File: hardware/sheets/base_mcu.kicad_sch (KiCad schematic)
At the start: 23 parts, among them J1 DevKit J1 (left row), J2 DevKit J3 (right row), J3 Qwiic, J4 Qwiic, J5 Expansion 2x10

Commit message: hardware: chip resistors and ceramic capacitors on KiCad standard footprints (Decision #47); schematic, library and gapped copies regenerated, ERC 0 errors
Co-Authored-By: Claude Fable 5.1 <noreply@anthropic.com>
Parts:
- R1, R2, R3, R4: footprint class_board:R0603 -> Resistor_SMD:R_0603_1608Metric
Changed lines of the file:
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@@
     (property "Reference" "R1" (at 55.88 171.958 0) (show_name no) (effects (font (size 1.27 1.27)) (justify left bottom)))
     (property "Value" "33" (at 55.88 178.562 0) (show_name no) (effects (font (size 1.27 1.27)) (justify left top)))
-    (property "Footprint" "class_board:R0603" (at 59.69 175.26 0) (show_name no) (effects (font (size 1.27 1.27)) (hide yes)))
+    (property "Footprint" "Resistor_SMD:R_0603_1608Metric" (at 59.69 175.26 0) (show_name no) (effects (font (size 1.27 1.27)) (hide yes)))
     (property "Datasheet" "https://www.lcsc.com/product-detail/C23140.html" (at 59.69 175.26 0) (show_name no) (effects (font (size 1.27 1.27)) (hide yes)))
     (property "Description" "Resistor 33 1% 0603 100 mW (Uniroyal 0603WAF330JT5E)" (at 59.69 175.26 0) (show_name no) (effects (font (size 1.27 1.27)) (hide yes)))
@@
     (property "Reference" "R2" (at 55.88 182.118 0) (show_name no) (effects (font (size 1.27 1.27)) (justify left bottom)))
     (property "Value" "33" (at 55.88 188.722 0) (show_name no) (effects (font (size 1.27 1.27)) (justify left top)))
-    (property "Footprint" "class_board:R0603" (at 59.69 185.42 0) (show_name no) (effects (font (size 1.27 1.27)) (hide yes)))
+    (property "Footprint" "Resistor_SMD:R_0603_1608Metric" (at 59.69 185.42 0) (show_name no) (effects (font (size 1.27 1.27)) (hide yes)))
     (property "Datasheet" "https://www.lcsc.com/product-detail/C23140.html" (at 59.69 185.42 0) (show_name no) (effects (font (size 1.27 1.27)) (hide yes)))
     (property "Description" "Resistor 33 1% 0603 100 mW (Uniroyal 0603WAF330JT5E)" (at 59.69 185.42 0) (show_name no) (effects (font (size 1.27 1.27)) (hide yes)))
@@
     (property "Reference" "R3" (at 247.65 55.118 0) (show_name no) (effects (font (size 1.27 1.27)) (justify left bottom)))
     (property "Value" "4.7k" (at 247.65 64.262 0) (show_name no) (effects (font (size 1.27 1.27)) (justify left top)))
-    (property "Footprint" "class_board:R0603" (at 250.19 59.69 0) (show_name no) (effects (font (size 1.27 1.27)) (hide yes)))
+    (property "Footprint" "Resistor_SMD:R_0603_1608Metric" (at 250.19 59.69 0) (show_name no) (effects (font (size 1.27 1.27)) (hide yes)))
     (property "Datasheet" "https://www.lcsc.com/product-detail/C23162.html" (at 250.19 59.69 0) (show_name no) (effects (font (size 1.27 1.27)) (hide yes)))
     (property "Description" "Resistor 4.7k 1% 0603 100 mW (Uniroyal 0603WAF4701T5E)" (at 250.19 59.69 0) (show_name no) (effects (font (size 1.27 1.27)) (hide yes)))
@@
     (property "Reference" "R4" (at 260.35 55.118 0) (show_name no) (effects (font (size 1.27 1.27)) (justify left bottom)))
     (property "Value" "4.7k" (at 260.35 64.262 0) (show_name no) (effects (font (size 1.27 1.27)) (justify left top)))
-    (property "Footprint" "class_board:R0603" (at 262.89 59.69 0) (show_name no) (effects (font (size 1.27 1.27)) (hide yes)))
+    (property "Footprint" "Resistor_SMD:R_0603_1608Metric" (at 262.89 59.69 0) (show_name no) (effects (font (size 1.27 1.27)) (hide yes)))
     (property "Datasheet" "https://www.lcsc.com/product-detail/C23162.html" (at 262.89 59.69 0) (show_name no) (effects (font (size 1.27 1.27)) (hide yes)))
     (property "Description" "Resistor 4.7k 1% 0603 100 mW (Uniroyal 0603WAF4701T5E)" (at 262.89 59.69 0) (show_name no) (effects (font (size 1.27 1.27)) (hide yes)))

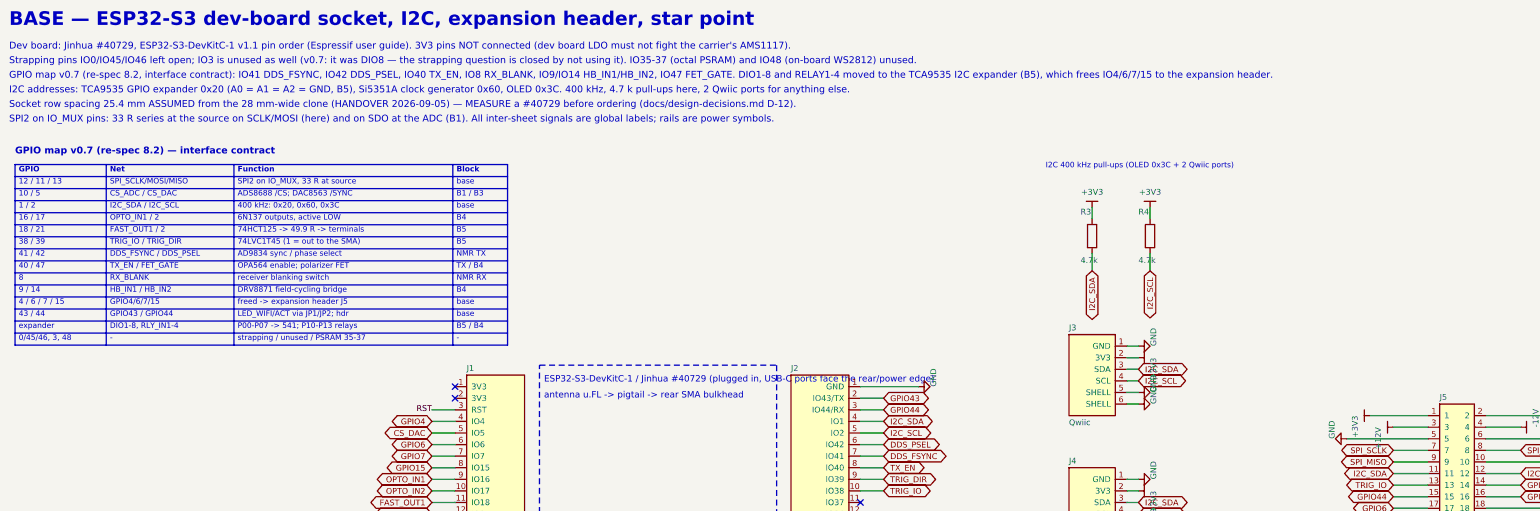
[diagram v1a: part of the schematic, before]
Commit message: hardware: panel stacked on the back (180 x 100, three 2x20 headers, 17 SMA, TTL strip, TX terminal, Qwiic); TTL/fast/TX-coil/Qwiic connectors leave the main board; mains-safe relay channels (JQC-3FF 10 A, MAINS net class + DRC rules); library, sheets, gapped copies, docs regenerated; ERC 0 errors
Decisions #45-#50 in the course repo. The main-board PCB is unchanged: Update PCB from Schematic, header placement, relay re-spacing and connector rotation are the instructor's GUI steps on the master.

Co-Authored-By: Claude Fable 5.1 <noreply@anthropic.com>
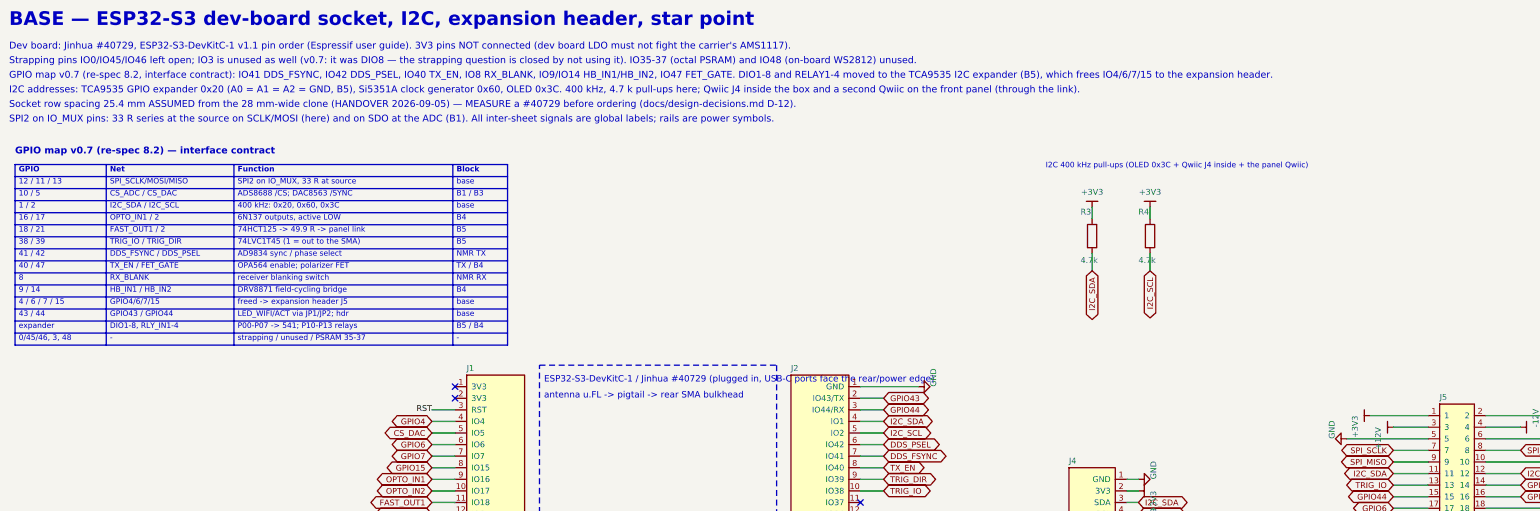
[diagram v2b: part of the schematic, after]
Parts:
- removed J3: Qwiic, class_board:CONN-SMD_4P-P1.00_XY-SM04B-SRSS-TB, symbol class_board:QWIIC_SM04B-SRSS
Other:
- note added: "74HCT125 -> 49.9 R -> panel link"
- note added: "I2C 400 kHz pull-ups (OLED 0x3C + Qwiic J4 inside + the panel Qwiic)"
- note added: "I2C addresses: TCA9535 GPIO expander 0x20 (A0 = A1 = A2 = GND, B5), Si5351A clock generator 0x60, OLED 0x3C. 400 kHz, 4.7 k pull-ups here; Qwiic J4 inside the box and a second Qwiic on the front panel (through the link)."
- note removed: "74HCT125 -> 49.9 R -> terminals"
- note removed: "I2C 400 kHz pull-ups (OLED 0x3C + 2 Qwiic ports)"
- note removed: "I2C addresses: TCA9535 GPIO expander 0x20 (A0 = A1 = A2 = GND, B5), Si5351A clock generator 0x60, OLED 0x3C. 400 kHz, 4.7 k pull-ups here, 2 Qwiic ports for anything else."

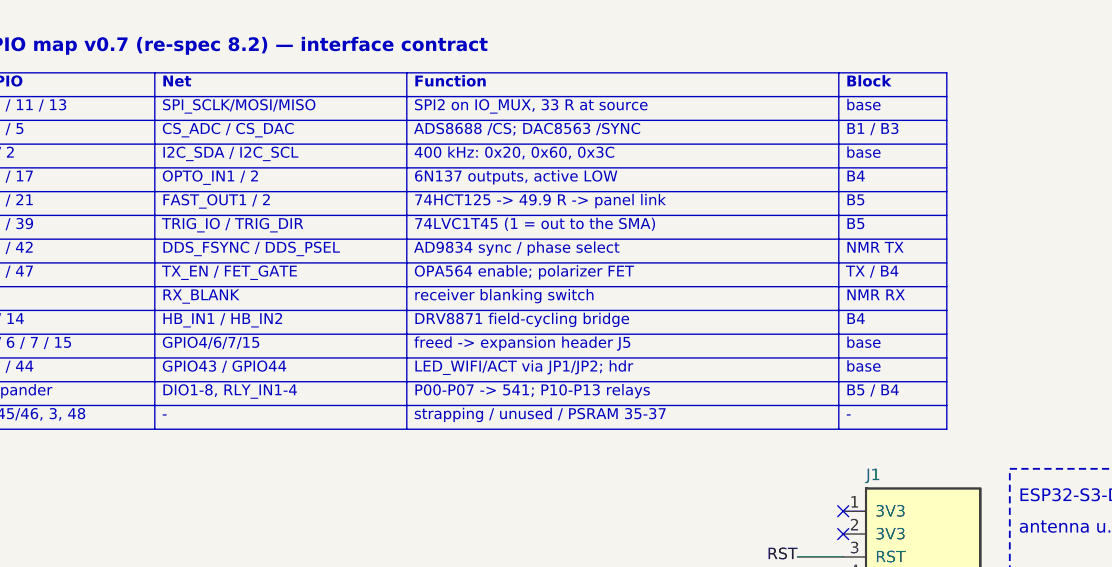
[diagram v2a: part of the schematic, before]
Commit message: v0.7d: relays and mains removed, MODULE OUT 1-7 (5 V TTL) on a shrouded 2x6 header on the front panel, isolated inputs moved to the panel, section C = the front-panel board (4-layer, 18 mm SMA grid, OLED clear of headers, unrouted student copy), main board re-placed; workbook, tutor guide, firmware docs, hardware docs updated (Decision #58)
Co-Authored-By: Claude Fable 5.1 <noreply@anthropic.com>
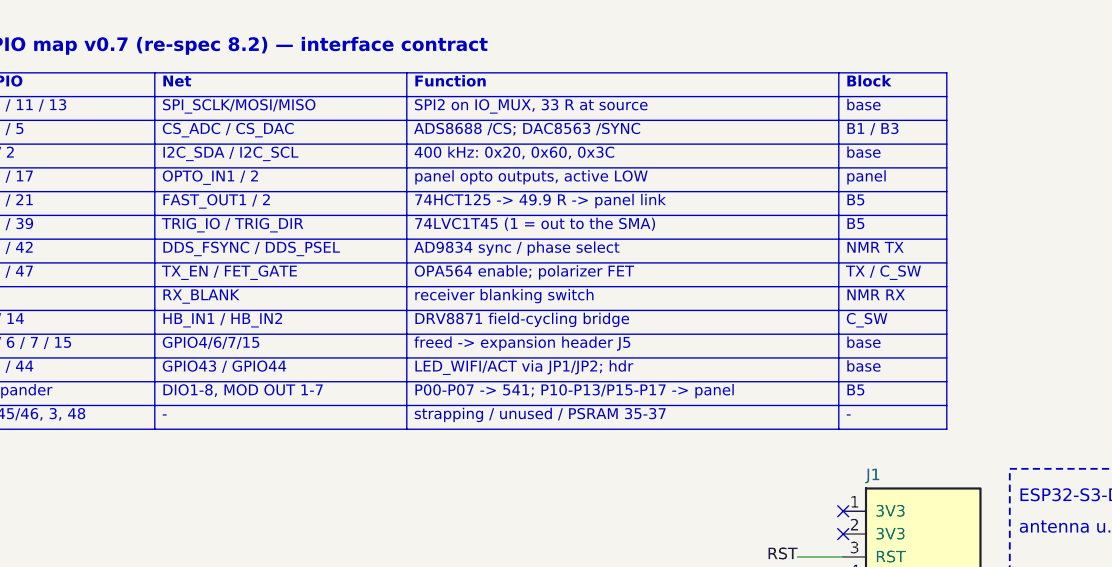
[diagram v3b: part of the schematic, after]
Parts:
- J5: footprint class_board:HDR-TH_20P-P2.54-V-M-R2-C10-S2.54 -> Connector_PinHeader_2.54mm:PinHeader_2x10_P2.54mm_Vertical
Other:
- note added: "C_SW"
- note added: "DIO1-8, MOD OUT 1-7"
- note added: "P00-P07 -> 541; P10-P13/P15-P17 -> panel"
- note added: "TX / C_SW"
- note added: "panel"
- note added: "panel opto outputs, active LOW"
- note removed: "6N137 outputs, active LOW"
- note removed: "B4"
- note removed: "B5 / B4"
- note removed: "DIO1-8, RLY_IN1-4"
- note removed: "P00-P07 -> 541; P10-P13 relays"
- note removed: "TX / B4"
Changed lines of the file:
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@@
   (text "16 / 17" (exclude_from_sim no) (at 14.8 56.4608 0) (effects (font (size 1.2 1.2)) (justify left bottom)))
   (text "OPTO_IN1 / 2" (exclude_from_sim no) (at 34.8 56.4608 0) (effects (font (size 1.2 1.2)) (justify left bottom)))
-  (text "6N137 outputs, active LOW" (exclude_from_sim no) (at 62.8 56.4608 0) (effects (font (size 1.2 1.2)) (justify left bottom)))
-  (text "B4" (exclude_from_sim no) (at 110.8 56.4608 0) (effects (font (size 1.2 1.2)) (justify left bottom)))
+  (text "panel opto outputs, active LOW" (exclude_from_sim no) (at 62.8 56.4608 0) (effects (font (size 1.2 1.2)) (justify left bottom)))
+  (text "panel" (exclude_from_sim no) (at 110.8 56.4608 0) (effects (font (size 1.2 1.2)) (justify left bottom)))
   (text "18 / 21" (exclude_from_sim no) (at 14.8 59.1008 0) (effects (font (size 1.2 1.2)) (justify left bottom)))
   (text "FAST_OUT1 / 2" (exclude_from_sim no) (at 34.8 59.1008 0) (effects (font (size 1.2 1.2)) (justify left bottom)))
@@
   (text "TX_EN / FET_GATE" (exclude_from_sim no) (at 34.8 67.0208 0) (effects (font (size 1.2 1.2)) (justify left bottom)))
   (text "OPA564 enable; polarizer FET" (exclude_from_sim no) (at 62.8 67.0208 0) (effects (font (size 1.2 1.2)) (justify left bottom)))
-  (text "TX / B4" (exclude_from_sim no) (at 110.8 67.0208 0) (effects (font (size 1.2 1.2)) (justify left bottom)))
+  (text "TX / C_SW" (exclude_from_sim no) (at 110.8 67.0208 0) (effects (font (size 1.2 1.2)) (justify left bottom)))
   (text "8" (exclude_from_sim no) (at 14.8 69.6608 0) (effects (font (size 1.2 1.2)) (justify left bottom)))
   (text "RX_BLANK" (exclude_from_sim no) (at 34.8 69.6608 0) (effects (font (size 1.2 1.2)) (justify left bottom)))
@@
   (text "HB_IN1 / HB_IN2" (exclude_from_sim no) (at 34.8 72.3008 0) (effects (font (size 1.2 1.2)) (justify left bottom)))
   (text "DRV8871 field-cycling bridge" (exclude_from_sim no) (at 62.8 72.3008 0) (effects (font (size 1.2 1.2)) (justify left bottom)))
-  (text "B4" (exclude_from_sim no) (at 110.8 72.3008 0) (effects (font (size 1.2 1.2)) (justify left bottom)))
+  (text "C_SW" (exclude_from_sim no) (at 110.8 72.3008 0) (effects (font (size 1.2 1.2)) (justify left bottom)))
   (text "4 / 6 / 7 / 15" (exclude_from_sim no) (at 14.8 74.9408 0) (effects (font (size 1.2 1.2)) (justify left bottom)))
   (text "GPIO4/6/7/15" (exclude_from_sim no) (at 34.8 74.9408 0) (effects (font (size 1.2 1.2)) (justify left bottom)))
@@
   (text "base" (exclude_from_sim no) (at 110.8 77.5808 0) (effects (font (size 1.2 1.2)) (justify left bottom)))
   (text "expander" (exclude_from_sim no) (at 14.8 80.2208 0) (effects (font (size 1.2 1.2)) (justify left bottom)))
-  (text "DIO1-8, RLY_IN1-4" (exclude_from_sim no) (at 34.8 80.2208 0) (effects (font (size 1.2 1.2)) (justify left bottom)))
-  (text "P00-P07 -> 541; P10-P13 relays" (exclude_from_sim no) (at 62.8 80.2208 0) (effects (font (size 1.2 1.2)) (justify left bottom)))
-  (text "B5 / B4" (exclude_from_sim no) (at 110.8 80.2208 0) (effects (font (size 1.2 1.2)) (justify left bottom)))
+  (text "DIO1-8, MOD OUT 1-7" (exclude_from_sim no) (at 34.8 80.2208 0) (effects (font (size 1.2 1.2)) (justify left bottom)))
+  (text "P00-P07 -> 541; P10-P13/P15-P17 -> panel" (exclude_from_sim no) (at 62.8 80.2208 0) (effects (font (size 1.2 1.2)) (justify left bottom)))
+  (text "B5" (exclude_from_sim no) (at 110.8 80.2208 0) (effects (font (size 1.2 1.2)) (justify left bottom)))
   (text "0/45/46, 3, 48" (exclude_from_sim no) (at 14.8 82.8608 0) (effects (font (size 1.2 1.2)) (justify left bottom)))
   (text "-" (exclude_from_sim no) (at 34.8 82.8608 0) (effects (font (size 1.2 1.2)) (justify left bottom)))
@@
     (property "Reference" "J5" (at 326.39 95.758 0) (show_name no) (effects (font (size 1.27 1.27)) (justify left bottom)))
     (property "Value" "Expansion 2x10" (at 326.39 125.222 0) (show_name no) (effects (font (size 1.27 1.27)) (justify left top)))
-    (property "Footprint" "class_board:HDR-TH_20P-P2.54-V-M-R2-C10-S2.54" (at 330.2 110.49 0) (show_name no) (effects (font (size 1.27 1.27)) (hide yes)))
+    (property "Footprint" "Connector_PinHeader_2.54mm:PinHeader_2x10_P2.54mm_Vertical" (at 330.2 110.49 0) (show_name no) (effects (font (size 1.27 1.27)) (hide yes)))
     (property "Datasheet" "https://www.lcsc.com/datasheet/lcsc_datasheet_2003191007_XFCN-PZ254V-12-20P_C492427.pdf" (at 330.2 110.49 0) (show_name no) (effects (font (size 1.27 1.27)) (hide yes)))
-    (property "Description" "2x10 straight male header (XFCN PZ254V-12-20P), expansion" (at 330.2 110.49 0) (show_name no) (effects (font (size 1.27 1.27)) (hide yes)))
+    (property "Description" "2x10 straight male header (XFCN PZ254V-12-20P), expansion. KiCad standard footprint (user 2026-09-17: generic 2.54 mm headers with good 3D models, real MPN and C-number in the fields)." (at 330.2 110.49 0) (show_name no) (effects (font (size 1.27 1.27)) (hide yes)))
     (property "LCSC" "C492427" (at 330.2 110.49 0) (show_name no) (effects (font (size 1.27 1.27)) (hide yes)))
     (property "JLC_CLASS" "Extended" (at 330.2 110.49 0) (show_name no) (effects (font (size 1.27 1.27)) (hide yes)))

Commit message: Schematic spacing rework: all nine sheets checker-clean, netlist fixes (LM66100 inputs off GND, TCXO divider joined), arrow rails, A2 for b5/c_switch/nmr_tx/nmr_rx; sch_check.py + net_diff.py; renders in docs/sch
Co-Authored-By: Claude Fable 5.1 <noreply@anthropic.com>
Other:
- note added: "ESP32-S3-DevKitC-1 /"
- note added: "Expansion header J5 (2x10), pinout D-17 v0.7:"
- note added: "GPIO map v0.7 (re-spec 8.2, interface contract): IO41 DDS_FSYNC, IO42 DDS_PSEL, IO40 TX_EN, IO8 RX_BLANK, IO9/IO14 HB_IN1/HB_IN2, IO47 FET_GATE. DIO1-8 and RELAY1-4 moved to the TCA9535"
- note added: "I2C addresses: TCA9535 GPIO expander 0x20 (A0 = A1 = A2 = GND, B5), Si5351A clock generator 0x60, OLED 0x3C. 400 kHz, 4.7 k pull-ups here; Qwiic J4 inside the box and a second Qwiic on"
- note added: "I2C expander (B5), which frees IO4/6/7/15 to the expansion header."
- note added: "JP2 when the TCXO option feeds GPIO44"
- note added: "Jinhua #40729, plugged in;"
- note added: "PWR_FLAGs: GND and AGND are references"
- note added: "Panel LED drive: bridged by default; open JP1 when the OPT chain uses GPIO43 as CS,"
- note added: "Placed at the B1/BASE boundary."
- note added: "Qwiic J4 (inside the box)"
- note added: "Rail test points"
- note added: "Strapping pins IO0/IO45/IO46 left open; IO3 is unused as well (v0.7: it was DIO8 — the strapping question is closed by not using it). IO35-37 (octal PSRAM) and IO48 (on-board WS2812)"
- note added: "The ONLY AGND-GND join (net tie NT1, copper only)."
- note added: "antenna u.FL -> pigtail ->"
- note added: "rear / power edge."
- note added: "rear SMA bulkhead"
- note added: "the USB-C ports face the"
- note added: "the four GPIO freed by the expander (4/6/7/15) took pins 16/17/19/20"
- note added: "the front panel (through the link)."
- note added: "unused."
- note added: "without a power_out driver"
- note removed: "ESP32-S3-DevKitC-1 / Jinhua #40729 (plugged in, USB-C ports face the rear/power edge)"
- note removed: "Expansion header J5 (2x10), pinout D-17 v0.7: the four GPIO freed by the expander (4/6/7/15) took pins 16/17/19/20"
- note removed: "GPIO map v0.7 (re-spec 8.2, interface contract): IO41 DDS_FSYNC, IO42 DDS_PSEL, IO40 TX_EN, IO8 RX_BLANK, IO9/IO14 HB_IN1/HB_IN2, IO47 FET_GATE. DIO1-8 and RELAY1-4 moved to the TCA9535 I2C expander (B5), which frees IO4/6/7/15 to the expansion header."
- note removed: "I2C addresses: TCA9535 GPIO expander 0x20 (A0 = A1 = A2 = GND, B5), Si5351A clock generator 0x60, OLED 0x3C. 400 kHz, 4.7 k pull-ups here; Qwiic J4 inside the box and a second Qwiic on the front panel (through the link)."
- note removed: "PWR_FLAGs: GND and AGND are references without a power_out driver"
- note removed: "Panel LED drive: bridged by default; open JP1 when the OPT chain uses GPIO43 as CS, JP2 when the TCXO option feeds GPIO44"
- note removed: "Strapping pins IO0/IO45/IO46 left open; IO3 is unused as well (v0.7: it was DIO8 — the strapping question is closed by not using it). IO35-37 (octal PSRAM) and IO48 (on-board WS2812) unused."
- note removed: "The ONLY AGND-GND join (net tie NT1, copper only). Placed at the B1/BASE boundary."
- note removed: "antenna u.FL -> pigtail -> rear SMA bulkhead"
- moved on the sheet: FID1, FID2, FID3, H1, H2, H3, H4, J1, J2, J4, JP1, JP2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
